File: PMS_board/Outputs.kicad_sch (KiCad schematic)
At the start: 107 parts, among them J10 AUX1, J11 AUX2, J12 D1, J13 D2, J14 D3, J15 D4, J16 T1, J17 T2, J18 T3, J19 T4, J4 Chopper_Shunt, J5 CORE, J6 DRIVE, J7 JET1, J8 JET2, J9 NET, U10 VN7140ASTR, U11 VN7140ASTR, U12 VN7140ASTR, U13 VN7007AHTR, U14 VN7007AHTR, U16 TLV7011DCKR, U17 LT1910, U25 IRFS7530TRL7PP, U26 IRFS7530TRL7PP, U27 IRFS7530TRL7PP, U28 LM74800QDRRRQ1, U29 IRFS7530TRL7PP, U30 IRFS7530TRL7PP, U31 LM74800QDRRRQ1

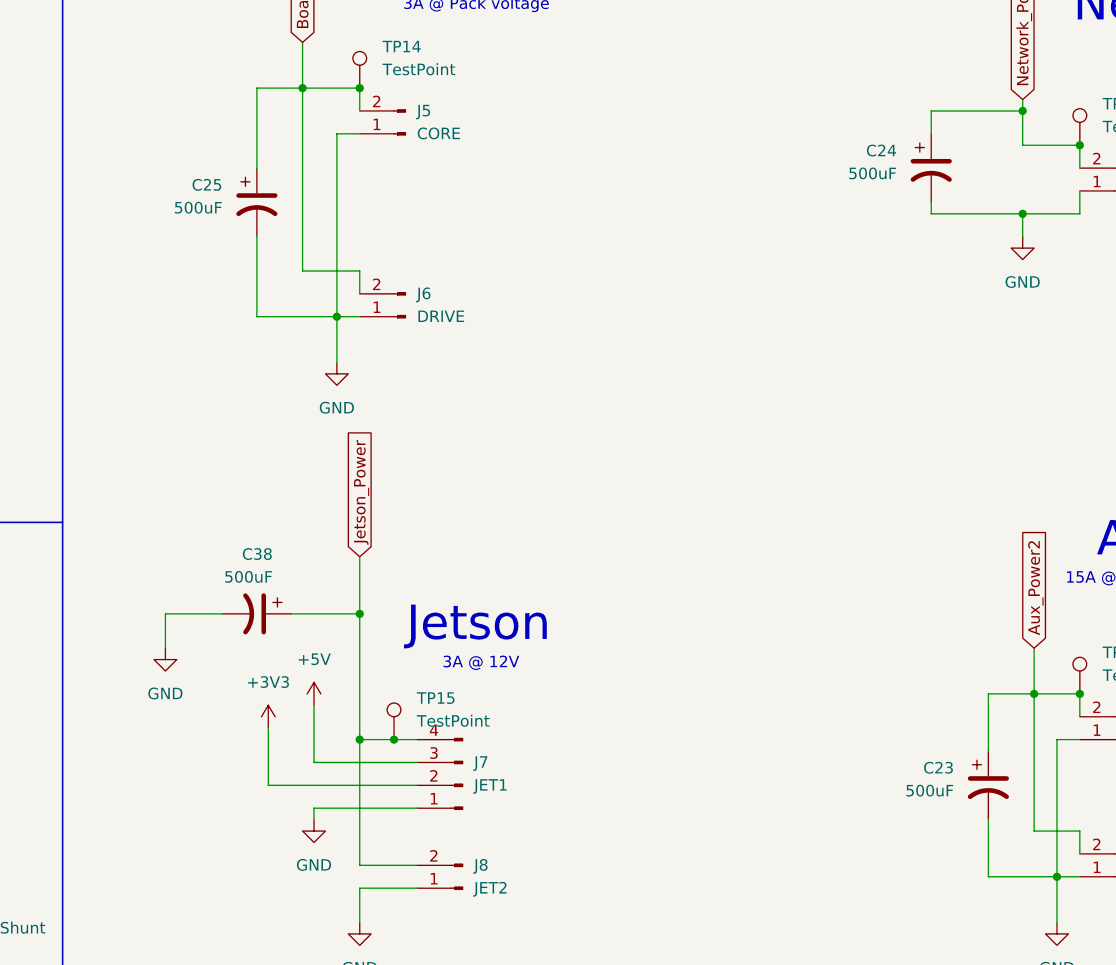
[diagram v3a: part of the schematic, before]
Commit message: Footprints for connectors and new resistors
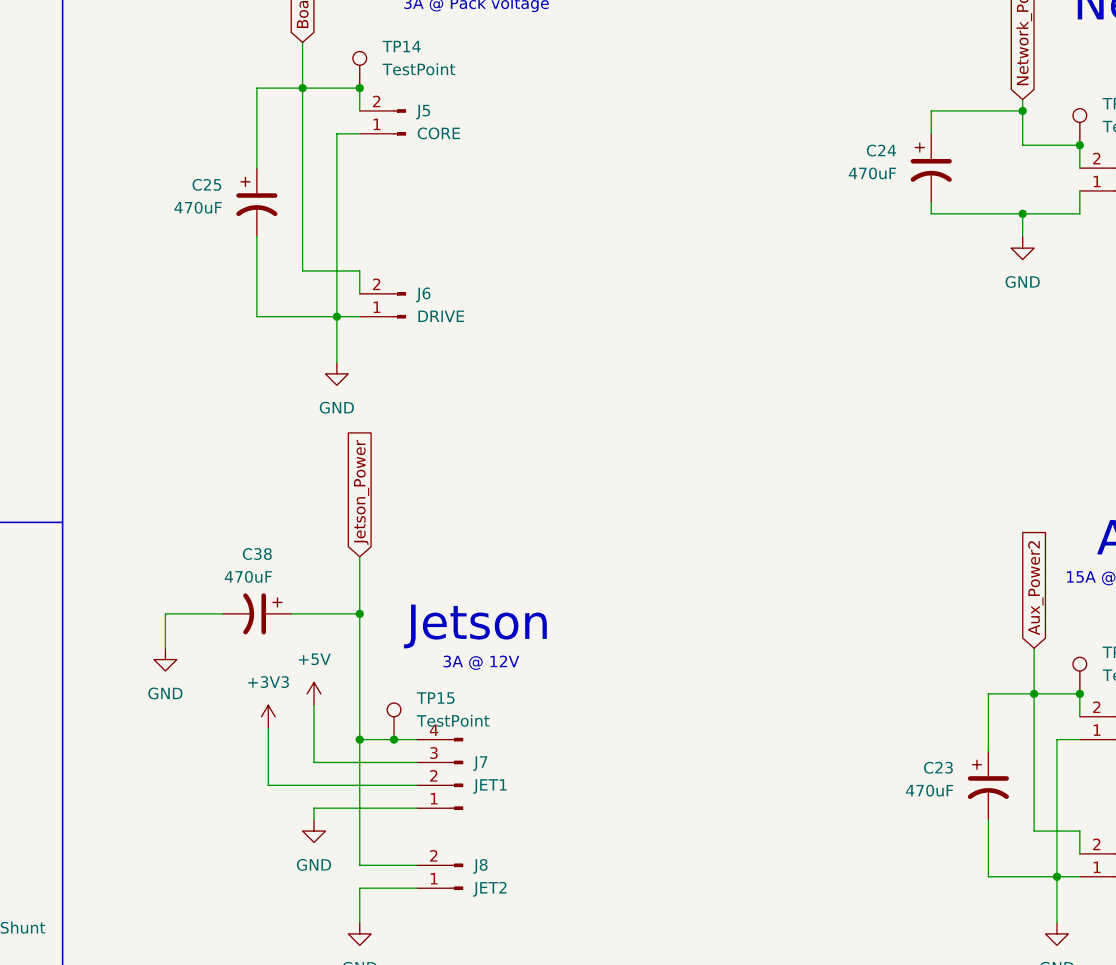
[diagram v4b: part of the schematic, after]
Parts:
- C23, C24, C25, C38: value 500uF -> 470uF
- J10, J11, J12, J13, J14, J15, J16, J17, J18, J19, J4, J5, J6, J7, J8, J9: footprint (none) -> MRDT_Connectors:MOLEX_MegaFit_02_Horizontal
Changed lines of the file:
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@@
 			)
 		)
-		(property "Footprint" ""
+		(property "Footprint" "MRDT_Connectors:MOLEX_MegaFit_02_Horizontal"
 			(at 490.22 99.06 0)
 			(hide yes)
@@
 			)
 		)
-		(property "Footprint" ""
+		(property "Footprint" "MRDT_Connectors:MOLEX_MegaFit_02_Horizontal"
 			(at 546.1 177.8 0)
 			(hide yes)
@@
 			)
 		)
-		(property "Footprint" ""
+		(property "Footprint" "MRDT_Connectors:MOLEX_MegaFit_02_Horizontal"
 			(at 410.21 92.71 0)
 			(hide yes)
@@
 			)
 		)
-		(property "Footprint" ""
+		(property "Footprint" "MRDT_Connectors:MOLEX_MegaFit_02_Horizontal"
 			(at 416.56 176.53 0)
 			(hide yes)
@@
 			)
 		)
-		(property "Value" "500uF"
+		(property "Value" "470uF"
 			(at 471.17 165.7349 0)
 			(show_name no)
@@
 			)
 		)
-		(property "Value" "500uF"
+		(property "Value" "470uF"
 			(at 395.478 141.986 90)
 			(show_name no)
@@
 			)
 		)
-		(property "Footprint" ""
+		(property "Footprint" "MRDT_Connectors:MOLEX_MegaFit_02_Horizontal"
 			(at 355.6 179.07 0)
 			(hide yes)
@@
 			)
 		)
-		(property "Footprint" ""
+		(property "Footprint" "MRDT_Connectors:MOLEX_MegaFit_02_Horizontal"
 			(at 546.1 191.77 0)
 			(hide yes)
@@
 			)
 		)
-		(property "Footprint" ""
+		(property "Footprint" "MRDT_Connectors:MOLEX_MegaFit_02_Horizontal"
 			(at 416.56 165.1 0)
 			(hide yes)
@@
 			)
 		)
-		(property "Footprint" ""
+		(property "Footprint" "MRDT_Connectors:MOLEX_MegaFit_02_Horizontal"
 			(at 410.21 113.03 0)
 			(hide yes)
@@
 			)
 		)
-		(property "Footprint" ""
+		(property "Footprint" "MRDT_Connectors:MOLEX_MegaFit_02_Horizontal"
 			(at 546.1 146.05 0)
 			(hide yes)
@@
 			)
 		)
-		(property "Footprint" ""
+		(property "Footprint" "MRDT_Connectors:MOLEX_MegaFit_02_Horizontal"
 			(at 546.1 78.74 0)
 			(hide yes)
@@
 			)
 		)
-		(property "Footprint" ""
+		(property "Footprint" "MRDT_Connectors:MOLEX_MegaFit_02_Horizontal"
 			(at 490.22 175.26 0)
 			(hide yes)
@@
 			)
 		)
-		(property "Footprint" ""
+		(property "Footprint" "MRDT_Connectors:MOLEX_MegaFit_02_Horizontal"
 			(at 546.1 165.1 0)
 			(hide yes)
@@
 			)
 		)
-		(property "Footprint" ""
+		(property "Footprint" "MRDT_Connectors:MOLEX_MegaFit_02_Horizontal"
 			(at 546.1 110.49 0)
 			(hide yes)
@@
 			)
 		)
-		(property "Footprint" ""
+		(property "Footprint" "MRDT_Connectors:MOLEX_MegaFit_02_Horizontal"
 			(at 490.22 160.02 0)
 			(hide yes)
@@
 			)
 		)
-		(property "Footprint" ""
+		(property "Footprint" "MRDT_Connectors:MOLEX_MegaFit_02_Horizontal"
 			(at 546.1 124.46 0)
 			(hide yes)
@@
 			)
 		)
-		(property "Value" "500uF"
+		(property "Value" "470uF"
 			(at 389.89 100.9649 0)
 			(show_name no)
@@
 			)
 		)
-		(property "Footprint" ""
+		(property "Footprint" "MRDT_Connectors:MOLEX_MegaFit_02_Horizontal"
 			(at 546.1 97.79 0)
 			(hide yes)
@@
 			)
 		)
-		(property "Value" "500uF"
+		(property "Value" "470uF"
 			(at 464.82 97.1549 0)
 			(show_name no)

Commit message: Add changes from Review
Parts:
- added V5: EMERGENCY_VIA, MRDT_Drill_Holes:BATT_PWR_VIA, symbol MRDT_Drill_Holes:BATT_PWR_VIA
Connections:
- net Motor_Power2: now also V5.1
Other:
- note added: "LEDS"
- note added: "LOAD SWITCHING"
- note added: "OUTPUTS"
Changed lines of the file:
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@@
 		)
 	)
+	(text "LOAD SWITCHING"
+		(exclude_from_sim no)
+		(at 106.68 24.384 0)
+		(effects
+			(font
+				(size 7.62 7.62)
+			)
+		)
+	)
+	(text ""
+		(exclude_from_sim no)
+		(at 107.696 14.986 0)
+		(effects
+			(font
+				(size 7.62 7.62)
+			)
+		)
+	)
 	(text "15A @ Pack voltage\nper motor"
 		(exclude_from_sim no)
@@
 		)
 	)
+	(text "LEDS"
+		(exclude_from_sim no)
+		(at 292.354 32.258 0)
+		(effects
+			(font
+				(size 7.62 7.62)
+			)
+		)
+	)
 	(text "Core/Drive\n"
 		(exclude_from_sim no)
@@
 		)
 	)
+	(text "OUTPUTS"
+		(exclude_from_sim no)
+		(at 487.934 35.052 0)
+		(effects
+			(font
+				(size 7 7)
+			)
+		)
+	)
 	(junction
 		(at 321.31 180.34)
@@
 	)
 	(junction
+		(at 528.32 57.15)
+		(diameter 0)
+		(color 0 0 0 0)
+	)
+	(junction
 		(at 57.15 201.93)
 		(diameter 0)
@@
 	(wire
 		(pts
+			(xy 528.32 46.99) (xy 528.32 57.15)
+		)
+		(stroke
+			(width 0)
+			(type default)
+		)
+	)
+	(wire
+		(pts
 			(xy 250.19 167.64) (xy 254 167.64)
 		)
@@
 	(wire
 		(pts
-			(xy 521.97 57.15) (xy 532.13 57.15)
+			(xy 521.97 57.15) (xy 528.32 57.15)
 		)
 		(stroke
@@
 	(wire
 		(pts
+			(xy 528.32 57.15) (xy 532.13 57.15)
+		)
+		(stroke
+			(width 0)
+			(type default)
+		)
+	)
+	(wire
+		(pts
 			(xy 67.31 154.94) (xy 67.31 156.21)
 		)
@@
 		)
 	)
-	(label "OUTPUTS"
-		(at 449.58 43.18 0)
-		(effects
-			(font
-				(size 7.62 7.62)
-			)
-			(justify left bottom)
-		)
-	)
 	(label "sourceC"
 		(at 194.31 302.26 0)
@@
 		)
 	)
-	(label "LEDS"
-		(at 275.59 43.18 0)
-		(effects
-			(font
-				(size 7.62 7.62)
-			)
-			(justify left bottom)
-		)
-	)
 	(label "DGateC"
 		(at 194.31 299.72 0)
@@
 		)
 	)
-	(label "LOAD SWITCHING"
-		(at 64.77 33.02 0)
-		(effects
-			(font
-				(size 7.62 7.62)
-			)
-			(justify left bottom)
-		)
-	)
 	(label "Dalmout"
 		(at 347.98 297.18 180)
@@
 					(unit 1)
 				)
+			)
+		)
+	)
+	(symbol
+		(lib_id "MRDT_Drill_Holes:BATT_PWR_VIA")
+		(at 528.32 41.91 0)
+		(unit 1)
+		(body_style 1)
+		(exclude_from_sim no)
+		(in_bom yes)
+		(on_board yes)
+		(in_pos_files yes)
+		(dnp no)
+		(fields_autoplaced yes)
+		(property "Reference" "V5"
+			(at 532.13 38.7349 0)
+			(show_name no)
+			(do_not_autoplace no)
+			(effects
+				(font
+					(size 1.524 1.524)
+				)
+				(justify left)
+			)
+		)
+		(property "Value" "EMERGENCY_VIA"
+			(at 532.13 41.2749 0)
+			(show_name no)
+			(do_not_autoplace no)
+			(effects
+				(font
+					(size 1.524 1.524)
+				)
+				(justify left)
+			)
+		)
+		(property "Footprint" "MRDT_Drill_Holes:BATT_PWR_VIA"
+			(at 528.32 41.91 0)
+			(hide yes)
+			(show_name no)
+			(do_not_autoplace no)
+			(effects
+				(font
+					(size 1.524 1.524)
+				)
+			)
+		)
+		(property "Datasheet" ""
+			(at 528.32 41.91 0)
+			(hide yes)
+			(show_name no)
+			(do_not_autoplace no)
+			(effects
+				(font
+					(size 1.524 1.524)
+				)
+			)
+		)
+		(property "Description" ""
+			(at 528.32 41.91 0)
+			(hide yes)
+			(show_name no)
+			(do_not_autoplace no)
+			(effects
+				(font
+					(size 1.27 1.27)
+				)
+			)
+		)
+		(property "KLC_S3.1" ""
+			(at 528.32 41.91 0)
+			(hide yes)
+			(show_name no)
+			(do_not_autoplace no)
+			(effects
+				(font
+					(size 1.27 1.27)
+				)
+			)
+		)
+		(property "KLC_S4.1" ""
+			(at 528.32 41.91 0)
+			(hide yes)
+			(show_name no)
+			(do_not_autoplace no)
+			(effects
+				(font
+					(size 1.27 1.27)
+				)
+			)
+		)
+		(property "KLC_S6.2" ""
+			(at 528.32 41.91 0)
+			(hide yes)
+			(show_name no)
+			(do_not_autoplace no)
+			(effects
+				(font
+					(size 1.27 1.27)
+				)
+			)
+		)
+		(pin "1"
+		)
+		(instances
+			(project "PMS_board"
+				(path "/282246b0-e0d8-4997-b3ee-58bf10355d52/266cb597-81f7-4ea7-87c1-e1b826fc674e"
+					(reference "V5")
+					(unit 1)
+				)

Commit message: Revert "Add changes from Review"
This reverts commit e7e7edd03615e33a608a50c27cdb501654904b7f.
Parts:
- removed V5: EMERGENCY_VIA, MRDT_Drill_Holes:BATT_PWR_VIA, symbol MRDT_Drill_Holes:BATT_PWR_VIA
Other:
- note removed: "LEDS"
- note removed: "LOAD SWITCHING"
- note removed: "OUTPUTS"
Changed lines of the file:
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@@
 		)
 	)
-	(text "LOAD SWITCHING"
-		(exclude_from_sim no)
-		(at 106.68 24.384 0)
-		(effects
-			(font
-				(size 7.62 7.62)
-			)
-		)
-	)
-	(text ""
-		(exclude_from_sim no)
-		(at 107.696 14.986 0)
-		(effects
-			(font
-				(size 7.62 7.62)
-			)
-		)
-	)
 	(text "15A @ Pack voltage\nper motor"
 		(exclude_from_sim no)
@@
 		)
 	)
-	(text "LEDS"
-		(exclude_from_sim no)
-		(at 292.354 32.258 0)
-		(effects
-			(font
-				(size 7.62 7.62)
-			)
-		)
-	)
 	(text "Core/Drive\n"
 		(exclude_from_sim no)
@@
 		)
 	)
-	(text "OUTPUTS"
-		(exclude_from_sim no)
-		(at 487.934 35.052 0)
-		(effects
-			(font
-				(size 7 7)
-			)
-		)
-	)
 	(junction
 		(at 321.31 180.34)
@@
 	)
 	(junction
-		(at 528.32 57.15)
-		(diameter 0)
-		(color 0 0 0 0)
-	)
-	(junction
 		(at 57.15 201.93)
 		(diameter 0)
@@
 	(wire
 		(pts
-			(xy 528.32 46.99) (xy 528.32 57.15)
-		)
-		(stroke
-			(width 0)
-			(type default)
-		)
-	)
-	(wire
-		(pts
 			(xy 250.19 167.64) (xy 254 167.64)
 		)
@@
 	(wire
 		(pts
-			(xy 521.97 57.15) (xy 528.32 57.15)
+			(xy 521.97 57.15) (xy 532.13 57.15)
 		)
 		(stroke
@@
 	(wire
 		(pts
-			(xy 528.32 57.15) (xy 532.13 57.15)
-		)
-		(stroke
-			(width 0)
-			(type default)
-		)
-	)
-	(wire
-		(pts
 			(xy 67.31 154.94) (xy 67.31 156.21)
 		)
@@
 		)
 	)
+	(label "OUTPUTS"
+		(at 449.58 43.18 0)
+		(effects
+			(font
+				(size 7.62 7.62)
+			)
+			(justify left bottom)
+		)
+	)
 	(label "sourceC"
 		(at 194.31 302.26 0)
@@
 		)
 	)
+	(label "LEDS"
+		(at 275.59 43.18 0)
+		(effects
+			(font
+				(size 7.62 7.62)
+			)
+			(justify left bottom)
+		)
+	)
 	(label "DGateC"
 		(at 194.31 299.72 0)
@@
 		)
 	)
+	(label "LOAD SWITCHING"
+		(at 64.77 33.02 0)
+		(effects
+			(font
+				(size 7.62 7.62)
+			)
+			(justify left bottom)
+		)
+	)
 	(label "Dalmout"
 		(at 347.98 297.18 180)
@@
 					(unit 1)
 				)
-			)
-		)
-	)
-	(symbol
-		(lib_id "MRDT_Drill_Holes:BATT_PWR_VIA")
-		(at 528.32 41.91 0)
-		(unit 1)
-		(body_style 1)
-		(exclude_from_sim no)
-		(in_bom yes)
-		(on_board yes)
-		(in_pos_files yes)
-		(dnp no)
-		(fields_autoplaced yes)
-		(property "Reference" "V5"
-			(at 532.13 38.7349 0)
-			(show_name no)
-			(do_not_autoplace no)
-			(effects
-				(font
-					(size 1.524 1.524)
-				)
-				(justify left)
-			)
-		)
-		(property "Value" "EMERGENCY_VIA"
-			(at 532.13 41.2749 0)
-			(show_name no)
-			(do_not_autoplace no)
-			(effects
-				(font
-					(size 1.524 1.524)
-				)
-				(justify left)
-			)
-		)
-		(property "Footprint" "MRDT_Drill_Holes:BATT_PWR_VIA"
-			(at 528.32 41.91 0)
-			(hide yes)
-			(show_name no)
-			(do_not_autoplace no)
-			(effects
-				(font
-					(size 1.524 1.524)
-				)
-			)
-		)
-		(property "Datasheet" ""
-			(at 528.32 41.91 0)
-			(hide yes)
-			(show_name no)
-			(do_not_autoplace no)
-			(effects
-				(font
-					(size 1.524 1.524)
-				)
-			)
-		)
-		(property "Description" ""
-			(at 528.32 41.91 0)
-			(hide yes)
-			(show_name no)
-			(do_not_autoplace no)
-			(effects
-				(font
-					(size 1.27 1.27)
-				)
-			)
-		)
-		(property "KLC_S3.1" ""
-			(at 528.32 41.91 0)
-			(hide yes)
-			(show_name no)
-			(do_not_autoplace no)
-			(effects
-				(font
-					(size 1.27 1.27)
-				)
-			)
-		)
-		(property "KLC_S4.1" ""
-			(at 528.32 41.91 0)
-			(hide yes)
-			(show_name no)
-			(do_not_autoplace no)
-			(effects
-				(font
-					(size 1.27 1.27)
-				)
-			)
-		)
-		(property "KLC_S6.2" ""
-			(at 528.32 41.91 0)
-			(hide yes)
-			(show_name no)
-			(do_not_autoplace no)
-			(effects
-				(font
-					(size 1.27 1.27)
-				)
-			)
-		)
-		(pin "1"
-		)
-		(instances
-			(project "PMS_board"
-				(path "/282246b0-e0d8-4997-b3ee-58bf10355d52/266cb597-81f7-4ea7-87c1-e1b826fc674e"
-					(reference "V5")
-					(unit 1)
-				)

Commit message: Voltage Sensing and Capacitor Assign
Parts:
- C23, C24, C25, C38: footprint (none) -> Capacitor_THT:CP_Radial_D10.0mm_P5.00mm
- C37: footprint (none) -> Capacitor_THT:CP_Radial_D16.0mm_P7.50mm
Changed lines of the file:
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@@
 			)
 		)
-		(property "Footprint" ""
+		(property "Footprint" "Capacitor_THT:CP_Radial_D10.0mm_P5.00mm"
 			(at 474.98 165.1 0)
 			(hide yes)
@@
 			)
 		)
-		(property "Datasheet" ""
+		(property "Datasheet" "https://mm.digikey.com/Volume0/opasdata/d220001/medias/docus/2452/ECA-xxM%20Series%2CTypeA.pdf"
 			(at 474.98 165.1 0)
 			(hide yes)
@@
 			)
 		)
-		(property "Description" "Polarized capacitor, US symbol"
+		(property "Description" "ECA-1HM471"
 			(at 474.98 165.1 0)
 			(hide yes)
@@
 			)
 		)
-		(property "Footprint" ""
+		(property "Footprint" "Capacitor_THT:CP_Radial_D16.0mm_P7.50mm"
 			(at 521.97 66.04 0)
 			(hide yes)
@@
 			)
 		)
-		(property "Datasheet" ""
+		(property "Datasheet" "https://www.rubycon.co.jp/wp-content/uploads/catalog-aluminum/ZLH.pdf"
 			(at 521.97 66.04 0)
 			(hide yes)
@@
 			)
 		)
-		(property "Description" "Polarized capacitor, US symbol"
+		(property "Description" "50ZLH1000MEFCGC16X25"
 			(at 521.97 66.04 0)
 			(hide yes)
@@
 			)
 		)
-		(property "Footprint" ""
+		(property "Footprint" "Capacitor_THT:CP_Radial_D10.0mm_P5.00mm"
 			(at 393.7 146.05 0)
 			(hide yes)
@@
 			)
 		)
-		(property "Datasheet" ""
+		(property "Datasheet" "https://mm.digikey.com/Volume0/opasdata/d220001/medias/docus/2452/ECA-xxM%20Series%2CTypeA.pdf"
 			(at 393.7 146.05 0)
 			(hide yes)
@@
 			)
 		)
-		(property "Description" "Polarized capacitor, US symbol"
+		(property "Description" "ECA-1HM471"
 			(at 393.7 146.05 0)
 			(hide yes)
@@
 			)
 		)
-		(property "Footprint" ""
+		(property "Footprint" "Capacitor_THT:CP_Radial_D10.0mm_P5.00mm"
 			(at 393.7 100.33 0)
 			(hide yes)
@@
 			)
 		)
-		(property "Datasheet" ""
+		(property "Datasheet" "https://mm.digikey.com/Volume0/opasdata/d220001/medias/docus/2452/ECA-xxM%20Series%2CTypeA.pdf"
 			(at 393.7 100.33 0)
 			(hide yes)
@@
 			)
 		)
-		(property "Description" "Polarized capacitor, US symbol"
+		(property "Description" "ECA-1HM471"
 			(at 393.7 100.33 0)
 			(hide yes)
@@
 			)
 		)
-		(property "Footprint" ""
+		(property "Footprint" "Capacitor_THT:CP_Radial_D10.0mm_P5.00mm"
 			(at 468.63 96.52 0)
 			(hide yes)
@@
 			)
 		)
-		(property "Datasheet" ""
+		(property "Datasheet" "https://mm.digikey.com/Volume0/opasdata/d220001/medias/docus/2452/ECA-xxM%20Series%2CTypeA.pdf"
 			(at 468.63 96.52 0)
 			(hide yes)
@@
 			)
 		)
-		(property "Description" "Polarized capacitor, US symbol"
+		(property "Description" "ECA-1HM471"
 			(at 468.63 96.52 0)
 			(hide yes)

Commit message: Refix Review Work
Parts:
- added V5: Jumper_Via, MRDT_Drill_Holes:BATT_PWR_VIA, symbol MRDT_Drill_Holes:BATT_PWR_VIA
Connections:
- net Motor_Power2: now also V5.1
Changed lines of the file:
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@@
 		(color 0 0 0 0)
 	)
+	(junction
+		(at 528.32 57.15)
+		(diameter 0)
+		(color 0 0 0 0)
+	)
 	(no_connect
 		(at 353.06 163.83)
@@
 	(wire
 		(pts
+			(xy 528.32 53.34) (xy 528.32 57.15)
+		)
+		(stroke
+			(width 0)
+			(type default)
+		)
+	)
+	(wire
+		(pts
 			(xy 181.61 256.54) (xy 181.61 259.08)
 		)
@@
 	(wire
 		(pts
+			(xy 528.32 57.15) (xy 532.13 57.15)
+		)
+		(stroke
+			(width 0)
+			(type default)
+		)
+	)
+	(wire
+		(pts
 			(xy 482.6 160.02) (xy 482.6 180.34)
 		)
@@
 	(wire
 		(pts
-			(xy 521.97 57.15) (xy 532.13 57.15)
+			(xy 521.97 57.15) (xy 528.32 57.15)
 		)
 		(stroke
@@
 					(unit 1)
 				)
+			)
+		)
+	)
+	(symbol
+		(lib_id "MRDT_Drill_Holes:BATT_PWR_VIA")
+		(at 528.32 48.26 0)
+		(unit 1)
+		(body_style 1)
+		(exclude_from_sim no)
+		(in_bom yes)
+		(on_board yes)
+		(in_pos_files yes)
+		(dnp no)
+		(fields_autoplaced yes)
+		(property "Reference" "V5"
+			(at 532.13 45.0849 0)
+			(show_name no)
+			(do_not_autoplace no)
+			(effects
+				(font
+					(size 1.524 1.524)
+				)
+				(justify left)
+			)
+		)
+		(property "Value" "Jumper_Via"
+			(at 532.13 47.6249 0)
+			(show_name no)
+			(do_not_autoplace no)
+			(effects
+				(font
+					(size 1.524 1.524)
+				)
+				(justify left)
+			)
+		)
+		(property "Footprint" "MRDT_Drill_Holes:BATT_PWR_VIA"
+			(at 528.32 48.26 0)
+			(hide yes)
+			(show_name no)
+			(do_not_autoplace no)
+			(effects
+				(font
+					(size 1.524 1.524)
+				)
+			)
+		)
+		(property "Datasheet" ""
+			(at 528.32 48.26 0)
+			(hide yes)
+			(show_name no)
+			(do_not_autoplace no)
+			(effects
+				(font
+					(size 1.524 1.524)
+				)
+			)
+		)
+		(property "Description" ""
+			(at 528.32 48.26 0)
+			(hide yes)
+			(show_name no)
+			(do_not_autoplace no)
+			(effects
+				(font
+					(size 1.27 1.27)
+				)
+			)
+		)
+		(property "KLC_S3.1" ""
+			(at 528.32 48.26 0)
+			(hide yes)
+			(show_name no)
+			(do_not_autoplace no)
+			(effects
+				(font
+					(size 1.27 1.27)
+				)
+			)
+		)
+		(property "KLC_S4.1" ""
+			(at 528.32 48.26 0)
+			(hide yes)
+			(show_name no)
+			(do_not_autoplace no)
+			(effects
+				(font
+					(size 1.27 1.27)
+				)
+			)
+		)
+		(property "KLC_S6.2" ""
+			(at 528.32 48.26 0)
+			(hide yes)
+			(show_name no)
+			(do_not_autoplace no)
+			(effects
+				(font
+					(size 1.27 1.27)
+				)
+			)
+		)
+		(pin "1"
+		)
+		(instances
+			(project "PMS_board"
+				(path "/282246b0-e0d8-4997-b3ee-58bf10355d52/266cb597-81f7-4ea7-87c1-e1b826fc674e"
+					(reference "V5")
+					(unit 1)
+				)
